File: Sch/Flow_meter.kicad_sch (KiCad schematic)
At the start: 26 parts

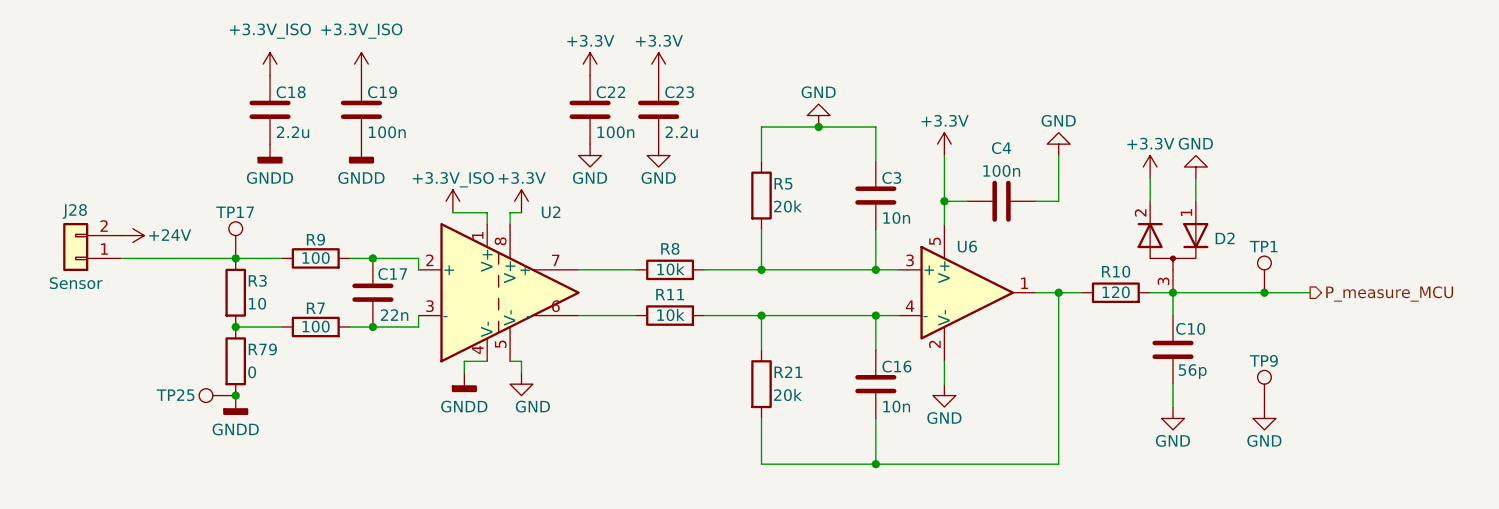
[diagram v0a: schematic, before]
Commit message: VER1.0: исправил каналы расходомеров, добавил папку с отчетным КД
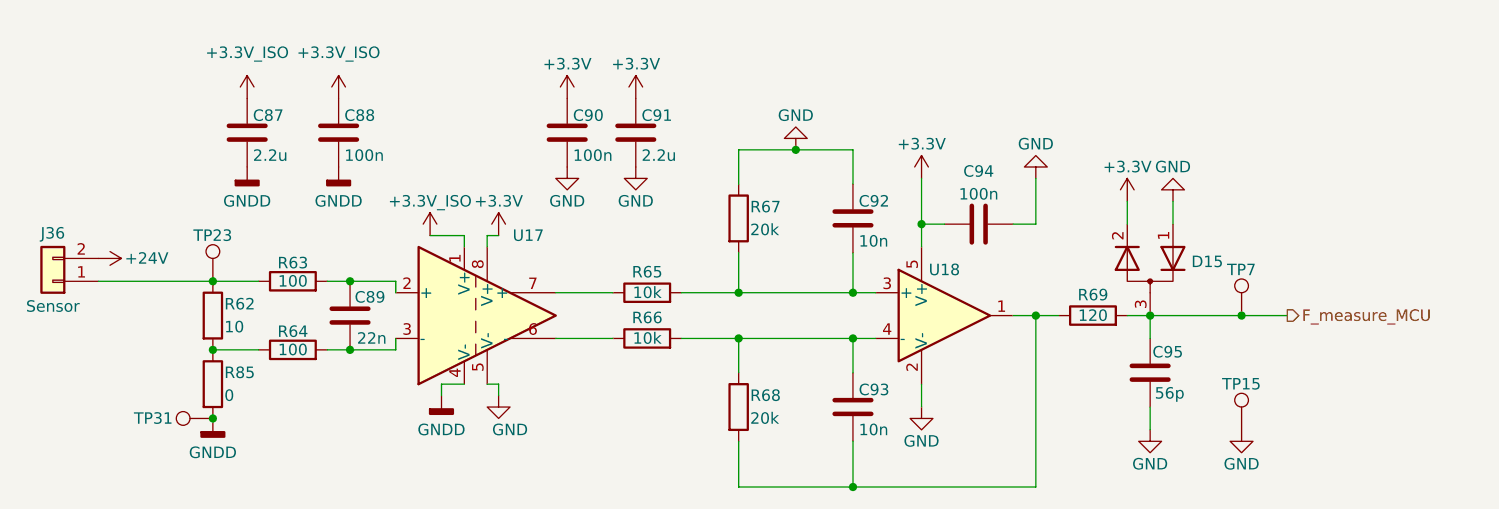
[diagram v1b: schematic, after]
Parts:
- removed C10: 56p, Capacitor_SMD:C_0805_2012Metric_Pad1.18x1.45mm_HandSolder, symbol Device:C
- removed C16, C3: 10n, Capacitor_SMD:C_0805_2012Metric_Pad1.18x1.45mm_HandSolder, symbol Device:C
- removed C17: 22n, Capacitor_SMD:C_0805_2012Metric_Pad1.18x1.45mm_HandSolder, symbol Device:C
- removed C18, C23: 2.2u, Capacitor_SMD:C_0805_2012Metric_Pad1.18x1.45mm_HandSolder, symbol Device:C
- removed C19, C22, C4: 100n, Capacitor_SMD:C_0805_2012Metric_Pad1.18x1.45mm_HandSolder, symbol Device:C
- removed D2: (no value), Package_TO_SOT_SMD:SOT-23, symbol Device:D_Dual_Series_AKC_Parallel
- removed J28: (no value), Connector_Molex:Molex_Mini-Fit_Jr_5569-02A2_2x01_P4.20mm_Horizontal, symbol Connector_Generic:Conn_01x02
- removed R10: 120, Resistor_SMD:R_0805_2012Metric_Pad1.20x1.40mm_HandSolder, symbol Device:R
- removed R11, R8: 10k, Resistor_SMD:R_0805_2012Metric_Pad1.20x1.40mm_HandSolder, symbol Device:R
- removed R21, R5: 20k, Resistor_SMD:R_0805_2012Metric_Pad1.20x1.40mm_HandSolder, symbol Device:R
- removed R3: 10, Resistor_SMD:R_1206_3216Metric_Pad1.30x1.75mm_HandSolder, symbol Device:R
- removed R7, R9: 100, Resistor_SMD:R_0805_2012Metric_Pad1.20x1.40mm_HandSolder, symbol Device:R
- removed R79: 0, Resistor_SMD:R_1206_3216Metric_Pad1.30x1.75mm_HandSolder, symbol Device:R
- removed TP1, TP17, TP25, TP9: TestPoint, TestPoint:TestPoint_Loop_D1.80mm_Drill1.0mm_Beaded, symbol Connector:TestPoint
- removed U2: (no value), Package_SO:SOIC-8_7.5x5.85mm_P1.27mm, symbol Amplifier_Difference:AMC1200BDWV
- removed U6: (no value), Package_TO_SOT_SMD:SOT-23-5, symbol Amplifier_Operational:OPA333xxDBV
- added C87, C91: 2.2u, Capacitor_SMD:C_0805_2012Metric_Pad1.18x1.45mm_HandSolder, symbol Device:C
- added C88, C90, C94: 100n, Capacitor_SMD:C_0805_2012Metric_Pad1.18x1.45mm_HandSolder, symbol Device:C
- added C89: 22n, Capacitor_SMD:C_0805_2012Metric_Pad1.18x1.45mm_HandSolder, symbol Device:C
- added C92, C93: 10n, Capacitor_SMD:C_0805_2012Metric_Pad1.18x1.45mm_HandSolder, symbol Device:C
- added C95: 56p, Capacitor_SMD:C_0805_2012Metric_Pad1.18x1.45mm_HandSolder, symbol Device:C
- added D15: (no value), Package_TO_SOT_SMD:SOT-23, symbol Device:D_Dual_Series_AKC_Parallel
- added J36: (no value), Connector_Molex:Molex_Mini-Fit_Jr_5569-02A2_2x01_P4.20mm_Horizontal, symbol Connector_Generic:Conn_01x02
- added R62: 10, Resistor_SMD:R_1206_3216Metric_Pad1.30x1.75mm_HandSolder, symbol Device:R
- added R63, R64: 100, Resistor_SMD:R_0805_2012Metric_Pad1.20x1.40mm_HandSolder, symbol Device:R
- added R65, R66: 10k, Resistor_SMD:R_0805_2012Metric_Pad1.20x1.40mm_HandSolder, symbol Device:R
- added R67, R68: 20k, Resistor_SMD:R_0805_2012Metric_Pad1.20x1.40mm_HandSolder, symbol Device:R
- added R69: 120, Resistor_SMD:R_0805_2012Metric_Pad1.20x1.40mm_HandSolder, symbol Device:R
- added R85: 0, Resistor_SMD:R_1206_3216Metric_Pad1.30x1.75mm_HandSolder, symbol Device:R
- added TP15, TP23, TP31, TP7: TestPoint, TestPoint:TestPoint_Loop_D1.80mm_Drill1.0mm_Beaded, symbol Connector:TestPoint
- added U17: (no value), Package_SO:SOIC-8_7.5x5.85mm_P1.27mm, symbol Amplifier_Difference:AMC1200BDWV
- added U18: (no value), Package_TO_SOT_SMD:SOT-23-5, symbol Amplifier_Operational:OPA333xxDBV
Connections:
- net +24V: now also J36.2 (Pin_2)
- net +3.3V: now also C90.1, C91.1, C94.1, D15.2 (K), U17.8 (V+), U18.5 (V+)
- net +3.3V_ISO: now also C87.1, C88.1, U17.1 (V+)
- net GND: now also C90.2, C91.2, C92.1, C94.2, C95.2, D15.1 (A), R67.1, TP15.1, U17.5 (V-), U18.2 (V-)
- net GNDD: now also C87.2, C88.2, R85.2, TP31.1, U17.4 (V-)
- new net: J36.1 (Pin_1), R62.1, R63.1, TP23.1
- new net: C89.1, R63.2, U17.2 (+)
- new net: C92.2, R65.2, R67.2, U18.3 (+)
- new net: R65.1, U17.7 (+)
- new net: C93.2, R68.2, R69.1, U18.1
- new net: C93.1, R66.2, R68.1, U18.4 (-)
- new net: R62.2, R64.1, R85.1
- new net: C89.2, R64.2, U17.3 (-)
- new net: R66.1, U17.6 (-)
- new net F_measure_MCU: C95.1, D15.3 (common), R69.2, TP7.1
